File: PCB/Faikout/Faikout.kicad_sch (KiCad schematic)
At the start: 44 parts, among them J1 S21, J2 TC2030-USB-NL, J3 Reset, Q1 BSS138PS, U4 ESP32-S3-MINI-1, U5 TPS62933

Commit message: As ordered
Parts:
- Q1: MPN C193381 -> C5224289; Rotation Offset (none) -> 90
- R16: MPN C158612 -> C473585
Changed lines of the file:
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@@
 			)
 		)
-		(property "MPN" "C193381"
+		(property "MPN" "C5224289"
 			(at 166.37 70.866 0)
 			(hide yes)
@@
 			)
 		)
+		(property "Rotation Offset" "90"
+			(at 156.845 76.835 0)
+			(hide yes)
+			(show_name no)
+			(do_not_autoplace no)
+			(effects
+				(font
+					(size 1.27 1.27)
+				)
+			)
+		)
 		(pin "1"
 		)
@@
 		(dnp no)
 		(property "Reference" "R16"
-			(at 114.3 171.704 90)
+			(at 114.3 172.212 90)
 			(show_name no)
 			(do_not_autoplace no)
@@
 			)
 		)
-		(property "MPN" "C158612"
+		(property "MPN" "C473585"
 			(at 114.3 170.18 0)
 			(hide yes)
@@
 		(property "Reference" "FID2"
 			(at 86.614 116.8978 0)
+			(hide yes)
 			(show_name no)
 			(do_not_autoplace no)
@@
 			)
 		)
-		(property "MPN" "C193381"
+		(property "MPN" "C5224289"
 			(at 152.4 114.681 0)
 			(hide yes)
@@
 			)
 		)
+		(property "Rotation Offset" "90"
+			(at 161.925 120.65 0)
+			(hide yes)
+			(show_name no)
+			(do_not_autoplace no)
+			(effects
+				(font
+					(size 1.27 1.27)
+				)
+			)
+		)
 		(pin "1"
 		)
@@
 		(property "Reference" "FID3"
 			(at 86.614 121.9778 0)
+			(hide yes)
 			(show_name no)
 			(do_not_autoplace no)

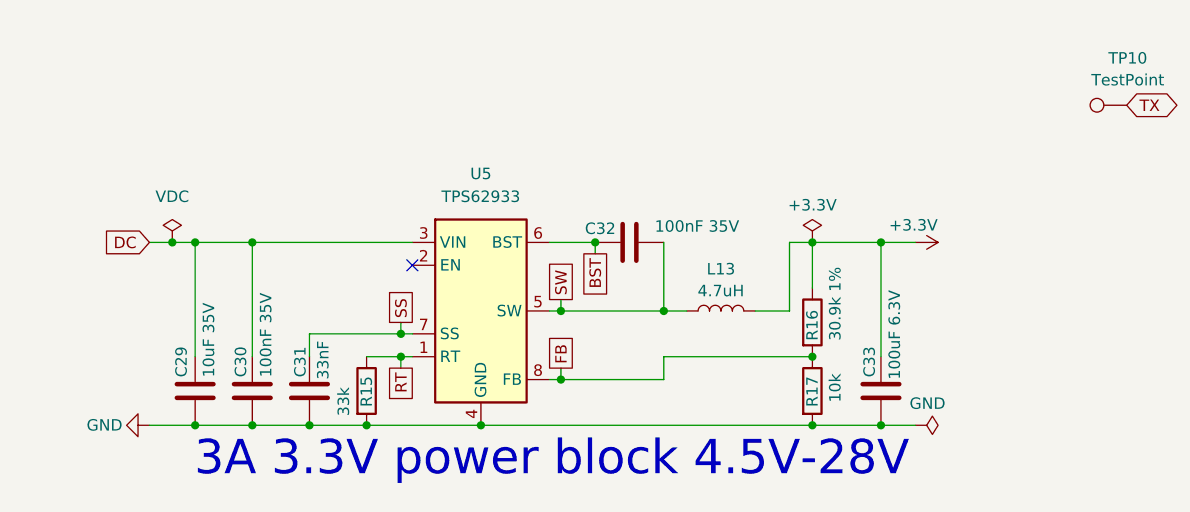
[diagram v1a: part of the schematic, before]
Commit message: New inductor
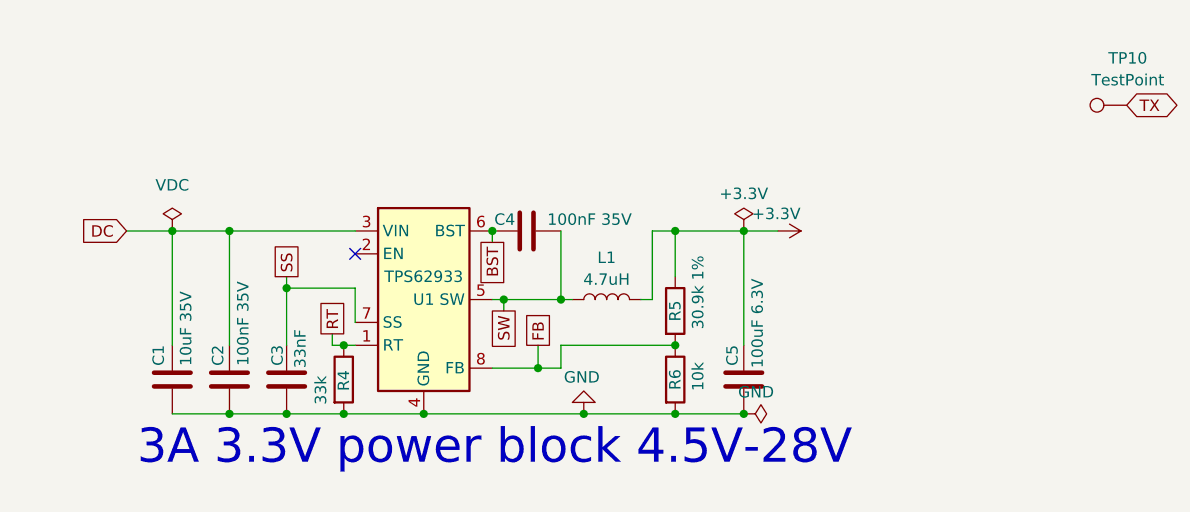
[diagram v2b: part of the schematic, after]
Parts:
- removed C29: 10uF 35V, RevK:C_0603, symbol Device:C
- removed C30, C32: 100nF 35V, RevK:C_0201, symbol Device:C
- removed C31: 33nF, RevK:C_0201, symbol Device:C
- removed C33: 100uF 6.3V, RevK:C_0805, symbol Device:C
- removed L13: 4.7uH, RevK:L_5x5, symbol Device:L
- removed R15: 33k, RevK:R_0201, symbol Device:R
- removed R16: 30.9k 1%, RevK:R_0201, symbol Device:R
- removed R17: 10k, RevK:R_0201, symbol Device:R
- removed U5: TPS62933, RevK:SOT-583-8, symbol Regulator_Switching:TPS62933
- added C1: 10uF 35V, RevK:C_0603, symbol Device:C
- added C2, C4: 100nF 35V, RevK:C_0201, symbol Device:C
- added C3: 33nF, RevK:C_0201, symbol Device:C
- added C5: 100uF 6.3V, RevK:C_0805, symbol Device:C
- added L1: 4.7uH, RevK:L_6x6, symbol Device:L
- added R4: 33k, RevK:R_0201, symbol Device:R
- added R5: 30.9k 1%, RevK:R_0201, symbol Device:R
- added R6: 10k, RevK:R_0201, symbol Device:R
- added U1: TPS62933, RevK:SOT-583-8, symbol Regulator_Switching:TPS62933
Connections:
- net +3.3V: now also C5.1, L1.2, R5.1
- net BST: now also C4.1, U1.6 (BST)
- net DC: now also C1.1, C2.1, U1.3 (VIN)
- net FB: now also R5.2, R6.1, U1.8 (FB)
- net GND: now also C1.2, C2.2, C3.2, C5.2, R4.2, R6.2, U1.4 (GND)
- net RT: now also R4.1, U1.1 (RT)
- net SS: now also C3.1, U1.7 (SS)
- net SW: now also C4.2, L1.1, U1.5 (SW)
